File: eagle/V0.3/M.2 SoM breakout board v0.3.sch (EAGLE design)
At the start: 137 parts, among them J1 3-PIN SMD, J11 WAFER-HY2.0-4PWB, J12 TP_OPEN, J13 SIM-NANO-4FF, J18 PARTICLE-STUDIOS_M_SERIES_M.2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, J19 TP_OPEN, J2 DCJ0202, J20 TP_OPEN, J21 SIP-2, J22 SIP-2, J3 SPARK_CON_30X2_SMD, J5 SCREW-HOLE-3.7, J6 PARTICLE-SZ_PARTICLE-POWER-MO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, J7 SCREW-HOLE-3.7, Q1 HSS2333, Q3 HSS2333, Q4 HSS2333, Q5 HSS2333, T1 TP_SHORT, U1 XC8107, U2 AT24CS64-SSHM-B, U7 NC, X1 BU-SMA-G, X2 BU-SMA-G, X3 BU-SMA-G

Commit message: update
update
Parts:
- removed J22: SIP-2, particle SZ:SIP-2
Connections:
- removed net VUSBMCU: J18G$1.NC@20, J22.1
- net CTS: now also JP25.2
- net GPIO1: no longer JP25.2
- net VUSB-MCU: now also J18G$1.NC@20; no longer J22.2
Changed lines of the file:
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@@
 <part name="D12" library="particle SZ" deviceset="ESD" device="" value="0402ESDA-05N"/>
 <part name="D13" library="particle SZ" deviceset="ESD" device="" value="0402ESDA-05N"/>
-<part name="J22" library="particle SZ" library_urn="urn:adsk.eagle:library:21650216" deviceset="SIP-2" device="" package3d_urn="urn:adsk.eagle:package:21650858/5"/>
 <part name="J21" library="particle SZ" library_urn="urn:adsk.eagle:library:21650216" deviceset="SIP-2" device="" package3d_urn="urn:adsk.eagle:package:21650858/5"/>
 <part name="R30" library="RedBear" deviceset="RES" device="R0603" value="100K"/>
@@
 <attribute name="VALUE" x="6.985" y="44.45" size="1.27" layer="96"/>
 </instance>
-<instance part="J22" gate="G$1" x="162.56" y="145.415" smashed="yes" rot="R90">
-<attribute name="NAME" x="158.115" y="147.955" size="1.27" layer="95"/>
-<attribute name="VALUE" x="161.29" y="147.955" size="1.27" layer="96"/>
-</instance>
 <instance part="J18" gate="G$1" x="118.745" y="106.68" smashed="yes">
 <attribute name="NAME" x="103.505" y="52.705" size="1.778" layer="95"/>
@@
 </segment>
 </net>
-<net name="VUSB-MCU" class="0">
-<segment>
-<wire x1="163.83" y1="139.7" x2="169.545" y2="139.7" width="0.1524" layer="91"/>
-<pinref part="J22" gate="G$1" pin="2"/>
-<wire x1="163.83" y1="140.335" x2="163.83" y2="139.7" width="0.1524" layer="91"/>
-<label x="169.545" y="139.7" size="1.27" layer="95" xref="yes"/>
-</segment>
-</net>
-<net name="VUSBMCU" class="0">
-<segment>
-<wire x1="144.145" y1="139.7" x2="161.29" y2="139.7" width="0.1524" layer="91"/>
-<pinref part="J22" gate="G$1" pin="1"/>
-<wire x1="161.29" y1="140.335" x2="161.29" y2="139.7" width="0.1524" layer="91"/>
-<pinref part="J18" gate="G$1" pin="NC@20"/>
-</segment>
-</net>
-<net name="N$10" class="0">
+<net name="VUSB_MCU" class="0">
 <segment>
 <wire x1="118.11" y1="106.68" x2="118.745" y2="106.68" width="0.1524" layer="91"/>
@@
 </segment>
 </net>
+<net name="VUSB-MCU" class="0">
+<segment>
+<wire x1="144.145" y1="139.7" x2="169.545" y2="139.7" width="0.1524" layer="91"/>
+<pinref part="J18" gate="G$1" pin="NC@20"/>
+<label x="169.545" y="139.7" size="1.27" layer="95" xref="yes"/>
+</segment>
+</net>
 </nets>
 </sheet>
@@
 <net name="GPIO1" class="0">
 <segment>
-<wire x1="227.33" y1="135.89" x2="239.395" y2="135.89" width="0.1524" layer="91"/>
-<label x="239.395" y="135.89" size="1.27" layer="95" xref="yes"/>
-<pinref part="JP25" gate="G$1" pin="2"/>
-</segment>
-<segment>
 <wire x1="181.61" y1="52.705" x2="192.405" y2="52.705" width="0.1524" layer="91"/>
 <label x="184.785" y="52.705" size="1.778" layer="95"/>
@@
 </segment>
 </net>
+<net name="CTS" class="0">
+<segment>
+<wire x1="227.33" y1="135.89" x2="239.395" y2="135.89" width="0.1524" layer="91"/>
+<label x="239.395" y="135.89" size="1.27" layer="95" xref="yes"/>
+<pinref part="JP25" gate="G$1" pin="2"/>
+</segment>
+</net>

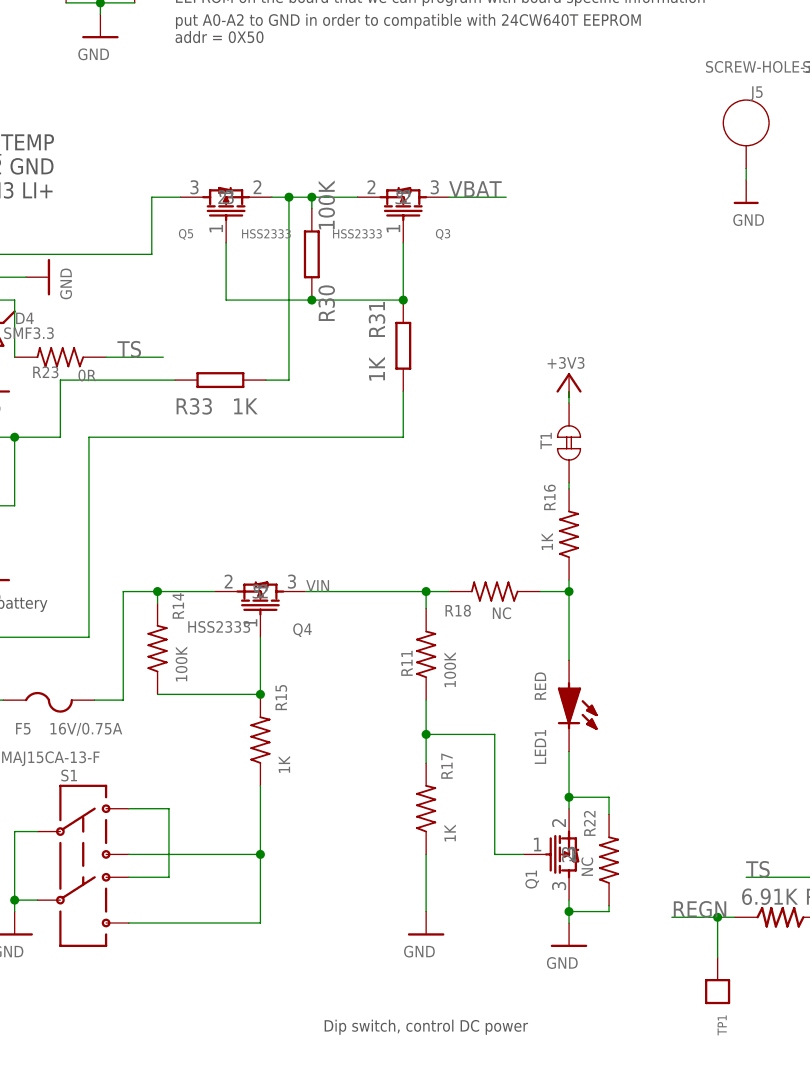
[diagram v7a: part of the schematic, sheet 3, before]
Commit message: update
1.Repair the silk screen to the jumper,change the size of the circle at the position of the small rubber pad
2.Remove the jumper from LED1 to 3V3,R16/NC,R17/NC.R11/NC, R22 as 0R ,make the circuit simple that used DC power supply directly  control, change the  Q1  as nmos and NC reserved
3.Optimize SPI traces to make them equal in length
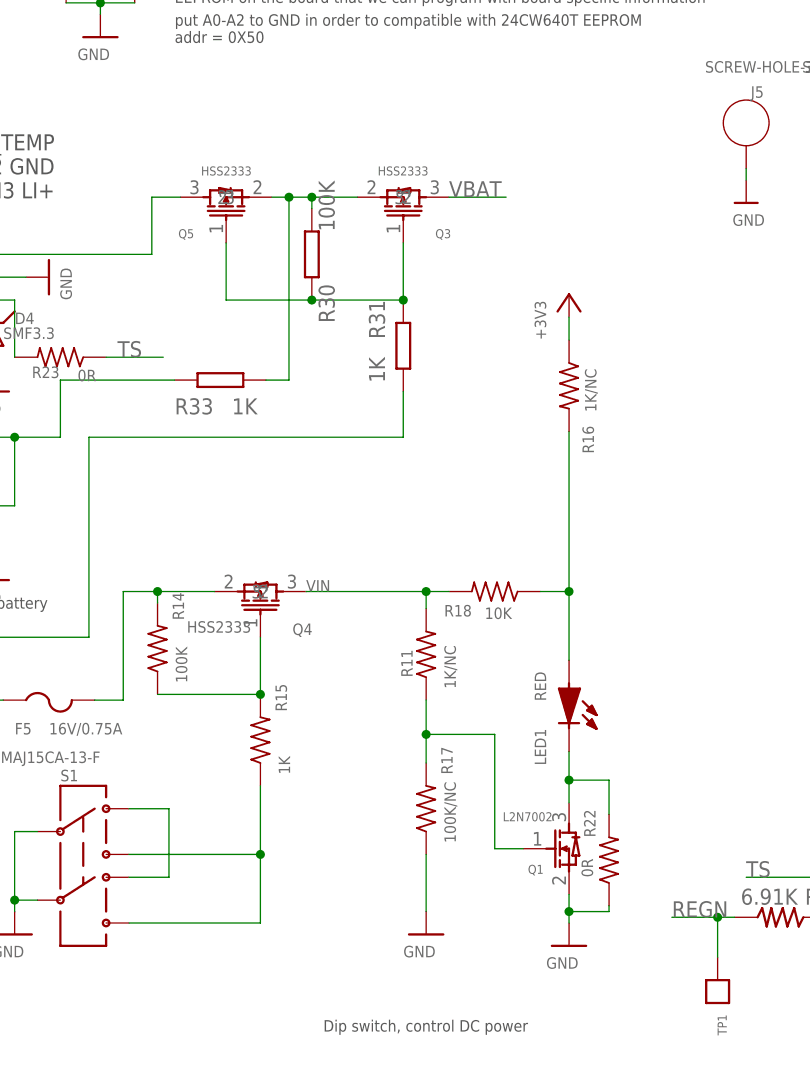
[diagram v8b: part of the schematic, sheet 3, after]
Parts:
- removed T1: TP_SHORT, particle SZ:TP_SHORT
- D16: value BZT52C3V9 -> PZ3D4V2H; device Diodes:MBR0520LT1G -> particle SZ:DIODESOD323
- F2: device RedBear:FUSEF1206 -> RedBear:FUSE
- Q1: value HSS2333 -> L2N7002; device RedBear:PMOS -> particle SZ:NMOSSOT323
- R11: value 100K -> 1K/NC
- R16: value 1K -> 1K/NC
- R17: value 1K -> 100K/NC
- R18: value NC -> 10K
- R22: value NC -> 0R
- RT1, RT2: device particle SZ:RESR0603 -> particle SZ:RESR0603A
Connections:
- removed net N$14: R16.2, T1.2
- net +3V3: now also R16.1; no longer T1.1
- net GND: now also D16.P$1, Q1.2; no longer D16.A, Q1.3
- net N$18: now also R16.2; no longer R16.1
- net N$36: now also Q1.3; no longer Q1.2
- net VCC: now also D16.P$2; no longer D16.C
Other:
- moved on the sheet: R16
